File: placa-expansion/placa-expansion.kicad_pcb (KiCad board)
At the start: 2 copper layers, 17 parts, among them J1 PBD-26, P1 BATT, P2 CONN_3PI, P3 PWR_HUB, P4 PWR_3pi, P5 CONN_4, P6 CONN_4, P7 CONN_4, P8 CONN_4, U1 PTN78020

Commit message: Comienzamos a rutear la placa interfaz
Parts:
- U1, U?1: moved to B.Cu
- moved P7 356.5 mm to (338.5, 257.5)
- moved P6 335.6 mm to (370.5, 189.0), turned to 90 degrees
- moved P2 329.2 mm to (338.5, 183.0)
- moved P3 328.8 mm to (366.5, 162.5), turned to 270 degrees
- moved U?1 318.2 mm to (324.0, 234.0), turned to 90 degrees
- moved P8 313.5 mm to (341.0, 151.0)
- moved R1 308.6 mm to (370.5, 173.5), turned to 90 degrees
- moved JP1 299.8 mm to (364.0, 153.5), turned to 90 degrees
- moved R2 293.8 mm to (308.0, 181.0), turned to 90 degrees
- moved D1 285.0 mm to (308.0, 191.5), turned to 90 degrees
- moved P5 280.2 mm to (308.0, 202.0), turned to 90 degrees
- moved C2 276.6 mm to (309.0, 161.5), turned to 180 degrees
- moved C1 273.3 mm to (317.0, 163.0), turned to 180 degrees
- moved P1 272.4 mm to (317.5, 156.0), turned to 180 degrees
- moved P4 262.7 mm to (308.0, 170.0), turned to 270 degrees
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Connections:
- J1 pad 7: (no net) -> /TX_rPi
- P2 pad 11: /PB3 -> /Echo4
- P2 pad 9: /Echo4 -> /PC6
- P4 pad 2: (no net) -> +BATT
- P5 pad 2: /PB3 -> /PC6
- P6 pad 2: /PB3 -> /PC6
- P7 pad 2: /PB3 -> /PC6
- P8 pad 2: /PB3 -> /PC6
- U?1 pad 13: /PB3 -> /PC6
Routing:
- net /TX_3pi: track 0.00 -> 123.6 mm
- net /AD6: track 0.00 -> 104.9 mm
- net /AD7: track 0.00 -> 91.5 mm
- net /Echo3: track 0.00 -> 78.0 mm
- net /RX_3pi: track 0.00 -> 71.1 mm
- net /Vcc_3pi: track 0.00 -> 59.0 mm
- net /Echo4: track 0.00 -> 58.7 mm
- net /PC6: track 0.00 -> 55.0 mm
- net /3v3_rPi: track 0.00 -> 31.3 mm
- net +5V: track 0.00 -> 27.4 mm
- net /TX_rPi: track 0.00 -> 17.0 mm
- net /LED: track 0.00 -> 16.7 mm
- net /PB3_rPi: track 0.00 -> 15.7 mm
- net /PC6_rPi: track 0.00 -> 14.0 mm
- net /AD6_rPi: track 0.00 -> 13.2 mm
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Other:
- board outline added: 139.1 x 220.7 mm
- net class Default: clearance 0.254 -> 0.4064; trace_width 0.254 -> 0.4064
- net class low_mils added: clearance 0.254, trace_width 0.3048, via_dia 0.889, via_drill 0.635
- rule trace_clearance: 0.254 -> 0.4064

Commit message: Pequeña modificacion en el pcb
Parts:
- moved P8 2.06 mm to (343.0, 150.5), turned to 180 degrees
- moved P5 0.50 mm to (308.0, 202.5), turned to 270 degrees
- turned R2 to 270 degrees
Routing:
- net /PC6: track 55.0 -> 319.8 mm
- net +5V: track 27.4 -> 117.4 mm
- net N-0000035: track 0.00 -> 66.8 mm
- net N-0000023: track 0.00 -> 40.1 mm
- net +BATT: track 0.00 -> 28.3 mm
- net N-0000022: track 0.00 -> 13.6 mm
- net /TX_3pi: track 123.6 -> 115.0 mm
- net N-000001: track 0.00 -> 4.15 mm
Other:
- outline, holes or cut-outs redrawn

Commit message: placa routeada
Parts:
- moved R1 201.0 mm to (185.3, 95.4), turned to 0 degrees
- moved C1 154.1 mm to (173.0, 108.1)
- moved C2 154.1 mm to (165.0, 106.6)
- moved D1 154.1 mm to (164.0, 136.6)
- moved J1 154.1 mm to (164.0, 180.6)
- moved P1 154.1 mm to (173.5, 101.1)
- moved P2 154.1 mm to (194.5, 128.1)
- moved P3 154.1 mm to (222.5, 107.6)
- moved P4 154.1 mm to (164.0, 115.1)
- moved P5 154.1 mm to (164.0, 147.6)
- moved P6 154.1 mm to (226.5, 134.1)
- moved P7 154.1 mm to (194.5, 202.6)
- moved P8 154.1 mm to (199.0, 95.6)
- moved R2 154.1 mm to (164.0, 126.1)
- moved U1 154.1 mm to (197.5, 109.1)
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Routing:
- net +5V: track 117.4 -> 269.3 mm, vias 0 -> 5
- net GND: track 0.00 -> 103.5 mm, vias 0 -> 13
- net /PC6: track 319.8 -> 218.2 mm, vias 0 -> 8
- net /Echo4: track 58.7 -> 139.5 mm, vias 0 -> 2
- net N-000002: track 0.00 -> 57.7 mm, vias 0 -> 1
- net /AD6: track 104.9 -> 159.6 mm, vias 0 -> 2
- net N-0000035: track 66.8 -> 30.2 mm
- net N-0000023: track 40.1 -> 7.30 mm
- net N-0000022: track 13.6 -> 44.4 mm
- net /Echo3: track 78.0 -> 105.0 mm, vias 0 -> 2
- net /RX_rPi: track 0.00 -> 16.5 mm
- net /AD7: track 91.5 -> 105.2 mm, vias 0 -> 2
- net /Vcc_3pi: track 59.0 -> 62.1 mm, vias 0 -> 2
- net /TX_3pi: track 115.0 -> 112.1 mm
- added copper zone on B.Cu, net GND
- added copper zone on F.Cu, net GND
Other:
- board size 139.1 x 220.7 mm -> 396.4 x 134.5 mm
- net class Default: clearance 0.4064 -> 0.3048; via_dia 0.889 -> 1.524
- net class low_mils: via_dia 0.889 -> 1.524
- rule trace_clearance: 0.4064 -> 0.3048

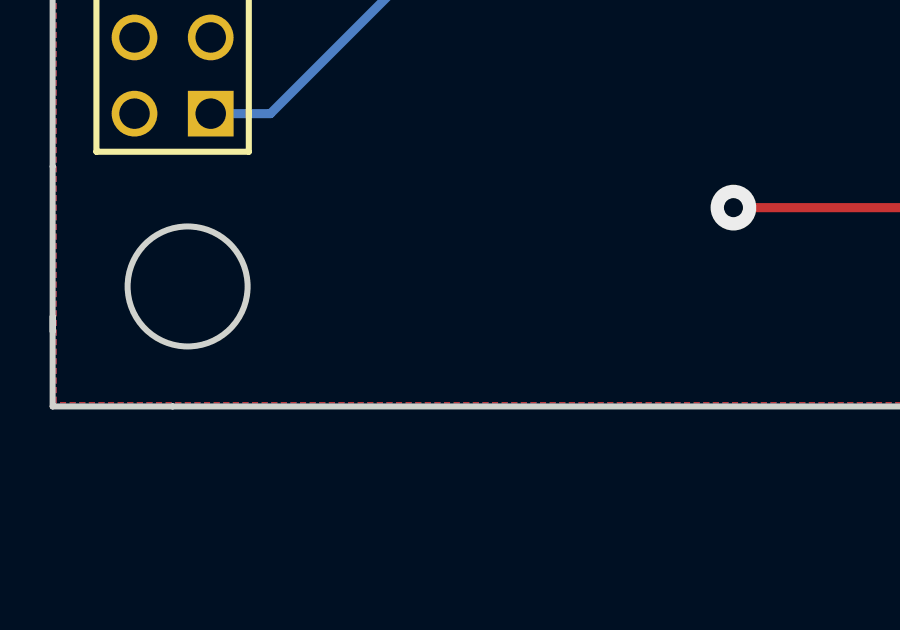
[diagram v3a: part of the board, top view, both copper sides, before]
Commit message: agregue texto a la placa
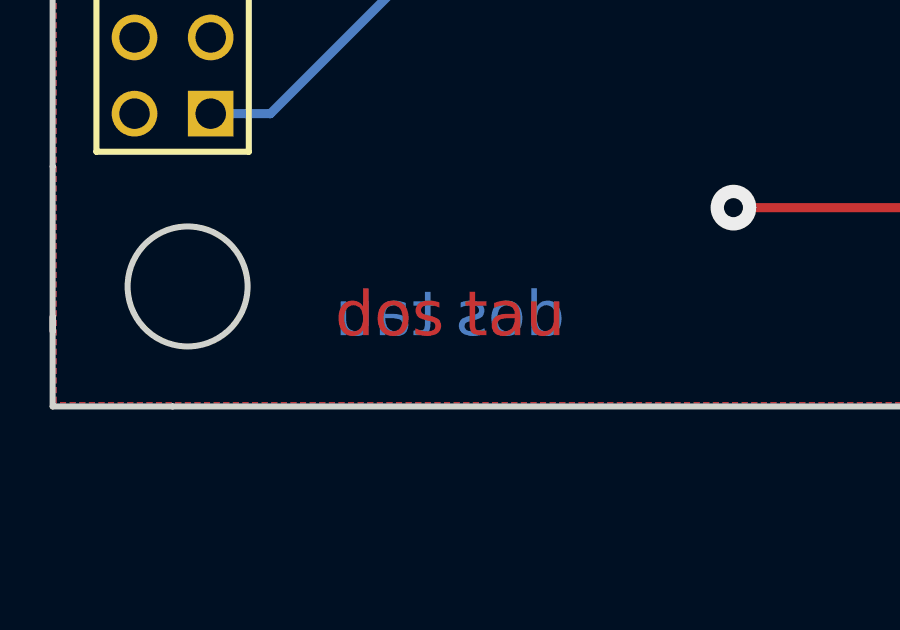
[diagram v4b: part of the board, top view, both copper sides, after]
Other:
- board text added: "dos tau"
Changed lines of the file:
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@@
     (links 59)
     (no_connects 0)
-    (area 232.640199 32.284999 538.580001 260.9544)
+    (area 159.2576 91.035999 573.073201 230.198601)
     (thickness 1.6)
-    (drawings 27)
+    (drawings 29)
     (tracks 270)
     (zones 0)
@@
     (visible_elements 7FFFEFFF)
     (pcbplotparams
-      (layerselection 3178497)
-      (usegerberextensions true)
-      (excludeedgelayer true)
+      (layerselection 32769)
+      (usegerberextensions false)
+      (excludeedgelayer false)
       (linewidth 0.150000)
       (plotframeref false)
@@
       (outputformat 1)
       (mirror false)
-      (drillshape 1)
+      (drillshape 0)
       (scaleselection 1)
       (outputdirectory ""))
@@
     )
   )
+  (gr_text "dos tau" (at 173.228 202.565) (layer F.Cu)
+    (effects (font (size 1.5 1.5) (thickness 0.3)))
+  )
+  (gr_text "dos tau" (at 173.228 202.565) (layer B.Cu)
+    (effects (font (size 1.5 1.5) (thickness 0.3)) (justify mirror))
+  )
   (gr_line (start 159.982 157.136) (end 159.982 160.136) (angle 90) (layer Edge.Cuts) (width 0.2))

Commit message: Borro las pistas y agrando los pads.
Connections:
- J1 pad 2: (no net) -> +5V
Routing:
- net +5V: track 269.3 -> 0.00 mm, vias 5 -> 0
- net /PC6: track 218.2 -> 0.00 mm, vias 8 -> 0
- net /AD6: track 159.6 -> 0.00 mm, vias 2 -> 0
- net /Echo4: track 139.5 -> 0.00 mm, vias 2 -> 0
- net /TX_3pi: track 112.1 -> 0.00 mm
- net /AD7: track 105.2 -> 0.00 mm, vias 2 -> 0
- net /Echo3: track 105.0 -> 0.00 mm, vias 2 -> 0
- net GND: track 103.5 -> 0.00 mm, vias 13 -> 0
- net /RX_3pi: track 71.1 -> 0.00 mm
- net /Vcc_3pi: track 62.1 -> 0.00 mm, vias 2 -> 0
- net N-000005: track 57.7 -> 0.00 mm, vias 1 -> 0
- net N-000001: track 44.4 -> 0.00 mm
- net /3v3_rPi: track 31.3 -> 0.00 mm
- net N-0000040: track 30.2 -> 0.00 mm
- net +BATT: track 28.3 -> 0.00 mm
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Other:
- board size 396.4 x 134.5 mm -> 70 x 114.2 mm
- net class Default: trace_width 0.4064 -> 0.8; via_dia 1.524 -> 2; via_drill 0.635 -> 0.8
- net class low_mils: trace_width 0.3048 -> 0.8; via_dia 1.524 -> 2; via_drill 0.635 -> 0.8

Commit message: subo placa rooteada. Faltaría revisión.
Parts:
- added 1PIN: P***, 1pin, F.Cu at (225.5, 202.1)
- added 1PIN: P***, 1pin, F.Cu at (164.5, 201.7)
- added 1PIN: P***, 1pin, F.Cu at (225.0, 159.1)
- added 1PIN: P***, 1pin, F.Cu at (165.0, 159.1)
- added 1PIN: P***, 1pin, F.Cu at (165.0, 100.2)
- added 1PIN: P***, 1pin, F.Cu at (225.0, 100.1)
- moved C2 55.3 mm to (219.0, 95.0), turned to 0 degrees
- moved JP1 46.7 mm to (173.5, 94.5), turned to 180 degrees
- moved R1 1.41 mm to (184.0, 96.0)
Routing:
- net /PC6: track 0.00 -> 270.9 mm, vias 0 -> 3
- net +5V: track 0.00 -> 240.7 mm, vias 0 -> 3
- net /Echo3: track 0.00 -> 173.0 mm, vias 0 -> 3
- net /Echo4: track 0.00 -> 136.1 mm, vias 0 -> 4
- net /TX_3pi: track 0.00 -> 106.0 mm, vias 0 -> 2
- net /AD7: track 0.00 -> 105.2 mm, vias 0 -> 3
- net /AD6: track 0.00 -> 105.2 mm, vias 0 -> 2
- net /RX_3pi: track 0.00 -> 92.4 mm, vias 0 -> 2
- net /Vcc_3pi: track 0.00 -> 60.3 mm
- net N-000005: track 0.00 -> 54.8 mm
- net N-000001: track 0.00 -> 47.5 mm
- net /RX_rPi: track 0.00 -> 46.4 mm, vias 0 -> 2
- net /3v3_rPi: track 0.00 -> 30.6 mm
- net +BATT: track 0.00 -> 29.4 mm
- net N-0000040: track 0.00 -> 24.5 mm
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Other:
- net class Default: clearance 0.3048 -> 0.508; trace_width 0.8 -> 0.762; via_drill 0.8 -> 0.7
- rule trace_clearance: 0.3048 -> 0.508

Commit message: subo logo a la placa
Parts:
- added G***: LOGO, LOGO, F.Cu at (220.9, 181.9)
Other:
- board text removed: "dos tau"
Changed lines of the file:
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@@
     (links 60)
     (no_connects 1)
-    (area 159.2576 91.149999 231.10022 206.0904)
+    (area 142.028571 90.6 231.30342 206.2936)
     (thickness 1.6)
-    (drawings 11)
+    (drawings 9)
     (tracks 279)
     (zones 0)
-    (modules 23)
+    (modules 24)
     (nets 26)
   )
@@
     (user_trace_width 0.508)
     (trace_clearance 0.508)
-    (zone_clearance 0.3048)
+    (zone_clearance 0.381)
     (zone_45_only no)
     (trace_min 0.254)
@@
     )
   )
+  (module LOGO (layer F.Cu)
+    (at 220.9 181.9 90)
+    (fp_text reference G*** (at 0 6.096 90) (layer F.SilkS) hide
+      (effects (font (thickness 0.3048)))
+    )
+    (fp_text value LOGO (at 0 -6.096 90) (layer F.SilkS) hide
+      (effects (font (thickness 0.3048)))
+    )
+    (fp_poly (pts (xy 13.63218 5.334) (xy 12.45362 5.334) (xy 12.45362 -4.32054) (xy 9.78662 -4.32054)
+      (xy 9.0424 -4.31546) (xy 8.36422 -4.30784) (xy 7.76986 -4.29514) (xy 7.28218 -4.27736)
+      (xy 6.92404 -4.2545) (xy 6.71068 -4.23164) (xy 6.70306 -4.2291) (xy 6.3246 -4.10464)
+      (xy 5.9944 -3.89128) (xy 5.69214 -3.57124) (xy 5.39242 -3.11912) (xy 5.15874 -2.68478)
+      (xy 4.97332 -2.31394) (xy 4.85902 -2.06502) (xy 4.80822 -1.91516) (xy 4.81076 -1.83642)
+      (xy 4.86156 -1.8034) (xy 4.90728 -1.79324) (xy 5.05206 -1.82626) (xy 5.25526 -1.9685)
+      (xy 5.53466 -2.23266) (xy 5.57276 -2.2733) (xy 5.87756 -2.56286) (xy 6.1595 -2.76098)
+      (xy 6.4643 -2.88036) (xy 6.83768 -2.94386) (xy 7.3279 -2.96418) (xy 7.4295 -2.96418)
+      (xy 7.69874 -2.96926) (xy 7.89178 -2.96418) (xy 8.02132 -2.92862) (xy 8.09244 -2.83972)
+      (xy 8.1153 -2.67208) (xy 8.10006 -2.40284) (xy 8.0518 -2.01168) (xy 7.99084 -1.5113)
+      (xy 7.91718 -0.77978) (xy 7.86638 -0.04064) (xy 7.84352 0.67564) (xy 7.84352 1.33858)
+      (xy 7.87146 1.91516) (xy 7.92226 2.37998) (xy 7.98068 2.64414) (xy 8.21436 3.18262)
+      (xy 8.53694 3.5814) (xy 8.9535 3.83794) (xy 9.47166 3.9624) (xy 9.7282 3.9751)
+      (xy 10.09396 3.95986) (xy 10.3759 3.89128) (xy 10.64006 3.76174) (xy 11.03122 3.43662)
+      (xy 11.34872 2.96418) (xy 11.59256 2.3495) (xy 11.73226 1.75514) (xy 11.75766 1.5494)
+      (xy 11.72464 1.45796) (xy 11.6078 1.43764) (xy 11.57986 1.43764) (xy 11.42492 1.47828)
+      (xy 11.29792 1.61798) (xy 11.21156 1.78816) (xy 10.96772 2.14884) (xy 10.62736 2.3749)
+      (xy 10.20826 2.45364) (xy 10.20318 2.45364) (xy 9.77392 2.37998) (xy 9.42848 2.16154)
+      (xy 9.17448 1.81102) (xy 9.02462 1.33858) (xy 9.00176 1.19126) (xy 8.9916 0.92456)
+      (xy 8.99922 0.52324) (xy 9.02716 0.01016) (xy 9.07034 -0.57658) (xy 9.12876 -1.21412)
+      (xy 9.19988 -1.8669) (xy 9.24306 -2.2225) (xy 9.3345 -2.96164) (xy 10.86866 -2.9845)
+      (xy 12.40282 -3.00736) (xy 12.42822 -3.66268) (xy 12.45362 -4.32054) (xy 12.45362 5.334)
+      (xy 2.1082 5.334) (xy 2.1082 -1.31318) (xy 1.92278 -1.3716) (xy 1.75514 -1.42494)
+      (xy 1.47828 -1.50876) (xy 1.14554 -1.60782) (xy 1.05918 -1.63576) (xy 0.381 -1.83642)
+      (xy 1.143 -2.06756) (xy 1.48844 -2.1717) (xy 1.77546 -2.25806) (xy 1.96596 -2.31648)
+      (xy 2.01168 -2.33172) (xy 2.05486 -2.39776) (xy 2.01422 -2.56032) (xy 1.9304 -2.75082)
+      (xy 1.81102 -2.96926) (xy 1.7145 -3.10896) (xy 1.67894 -3.13436) (xy 1.58496 -3.09372)
+      (xy 1.37668 -2.97942) (xy 1.0922 -2.81686) (xy 0.8382 -2.66446) (xy 0.5207 -2.47396)
+      (xy 0.26162 -2.32664) (xy 0.09398 -2.23774) (xy 0.04064 -2.21996) (xy 0.04318 -2.30886)
+      (xy 0.06604 -2.5273) (xy 0.10922 -2.83464) (xy 0.13462 -3.00736) (xy 0.18542 -3.35026)
+      (xy 0.22606 -3.62712) (xy 0.24892 -3.79984) (xy 0.25146 -3.83286) (xy 0.17526 -3.86842)
+      (xy -0.02032 -3.89128) (xy -0.21336 -3.89636) (xy -0.48006 -3.89128) (xy -0.61214 -3.86588)
+      (xy -0.65278 -3.79984) (xy -0.64008 -3.70586) (xy -0.59944 -3.48996) (xy -0.55626 -3.2004)
+      (xy -0.51562 -2.8829) (xy -0.4826 -2.58572) (xy -0.46228 -2.35204) (xy -0.45974 -2.22758)
+      (xy -0.46228 -2.21996) (xy -0.54102 -2.25044) (xy -0.73406 -2.35458) (xy -1.00838 -2.51714)
+      (xy -1.3081 -2.70256) (xy -2.1209 -3.21564) (xy -2.30632 -2.83718) (xy -2.41046 -2.57302)
+      (xy -2.4257 -2.40792) (xy -2.40792 -2.37998) (xy -2.29616 -2.3241) (xy -2.06248 -2.2352)
+      (xy -1.74752 -2.12852) (xy -1.56718 -2.07264) (xy -0.80518 -1.83896) (xy -1.60782 -1.5875)
+      (xy -1.95072 -1.48082) (xy -2.22758 -1.38938) (xy -2.40284 -1.32842) (xy -2.44348 -1.31064)
+      (xy -2.43586 -1.2192) (xy -2.37744 -1.03632) (xy -2.29362 -0.81788) (xy -2.20472 -0.62484)
+      (xy -2.13614 -0.51562) (xy -2.12344 -0.508) (xy -2.032 -0.55118) (xy -1.8288 -0.66548)
+      (xy -1.54432 -0.83312) (xy -1.23444 -1.02108) (xy -0.40386 -1.53416) (xy -0.45212 -1.25476)
+      (xy -0.49276 -0.99568) (xy -0.53594 -0.67564) (xy -0.55118 -0.55118) (xy -0.58928 -0.26162)
+      (xy -0.62738 -0.01524) (xy -0.64262 0.0635) (xy -0.65278 0.17018) (xy -0.59944 0.2286)
+      (xy -0.4445 0.24892) (xy -0.21336 0.254) (xy 0.08128 0.23876) (xy 0.2286 0.1905)
+      (xy 0.254 0.14224) (xy 0.23876 0.00254) (xy 0.20574 -0.24384) (xy 0.16764 -0.47244)
+      (xy 0.11176 -0.8001) (xy 0.06096 -1.10236) (xy 0.03556 -1.24968) (xy -0.00762 -1.524)
+      (xy 0.84836 -1.00838) (xy 1.18364 -0.81026) (xy 1.46304 -0.65278) (xy 1.65862 -0.55118)
+      (xy 1.73736 -0.52578) (xy 1.78816 -0.61468) (xy 1.8796 -0.80772) (xy 1.94056 -0.93472)
+      (xy 2.1082 -1.31318) (xy 2.1082 5.334) (xy 0.04318 5.334) (xy -6.62178 5.334)
+      (xy -6.62178 -2.48158) (xy -6.65734 -2.81178) (xy -6.6802 -2.8956) (xy -6.87578 -3.24866)
+      (xy -7.19074 -3.5687) (xy -7.58444 -3.80492) (xy -7.69366 -3.85064) (xy -8.001 -3.91922)
+      (xy -8.42264 -3.95986) (xy -8.90524 -3.97256) (xy -9.40054 -3.95732) (xy -9.85266 -3.91414)
+      (xy -10.11682 -3.86588) (xy -10.53846 -3.76936) (xy -10.64006 -3.175) (xy -10.7061 -2.78384)
+      (xy -10.73658 -2.5273) (xy -10.73404 -2.37744) (xy -10.69086 -2.30886) (xy -10.6045 -2.28854)
+      (xy -10.56132 -2.286) (xy -10.43432 -2.32156) (xy -10.32764 -2.44602) (xy -10.21334 -2.69748)
+      (xy -10.1981 -2.7305) (xy -10.04824 -3.03784) (xy -9.8552 -3.24358) (xy -9.58342 -3.37058)
+      (xy -9.1948 -3.43916) (xy -8.9662 -3.45694) (xy -8.56996 -3.45948) (xy -8.28294 -3.41122)
+      (xy -8.13562 -3.34772) (xy -7.8613 -3.11658) (xy -7.69366 -2.77368) (xy -7.63016 -2.33934)
+      (xy -7.67334 -1.83642) (xy -7.82574 -1.28778) (xy -8.001 -0.8763) (xy -8.20674 -0.51308)
+      (xy -8.46074 -0.15748) (xy -8.7884 0.2032) (xy -9.20242 0.59182) (xy -9.72058 1.02362)
+      (xy -10.36066 1.51384) (xy -10.62482 1.70942) (xy -11.09218 2.05486) (xy -11.43762 2.32156)
+      (xy -11.68146 2.53238) (xy -11.84148 2.70764) (xy -11.938 2.86766) (xy -11.9888 3.0353)
+      (xy -12.00912 3.22834) (xy -12.0142 3.27914) (xy -12.02182 3.46964) (xy -9.73582 3.46964)
+      (xy -9.02208 3.4671) (xy -8.46328 3.46202) (xy -8.04164 3.45186) (xy -7.747 3.43662)
+      (xy -7.55904 3.4163) (xy -7.4676 3.38836) (xy -7.44982 3.3655) (xy -7.43712 3.21564)
+      (xy -7.4041 2.9845) (xy -7.39648 2.94132) (xy -7.34568 2.62636) (xy -9.1821 2.6035)
+      (xy -11.01852 2.58064) (xy -10.0711 1.91262) (xy -9.22528 1.29794) (xy -8.52424 0.74422)
+      (xy -7.9502 0.23622) (xy -7.49554 -0.23368) (xy -7.1501 -0.6858) (xy -6.89864 -1.12776)
+      (xy -6.73354 -1.57226) (xy -6.6421 -2.03708) (xy -6.63448 -2.09804) (xy -6.62178 -2.48158)
+      (xy -6.62178 5.334) (xy -13.54582 5.334) (xy -13.54582 0) (xy -13.54582 -5.334)
+      (xy 0.04318 -5.334) (xy 13.63218 -5.334) (xy 13.63218 0) (xy 13.63218 5.334)
+      (xy 13.63218 5.334)) (layer F.Cu) (width 0.00254))
+  )
   (gr_line (start 160 205.5) (end 160 91.25) (angle 90) (layer Edge.Cuts) (width 0.2))
   (gr_line (start 230 205.5) (end 160 205.5) (angle 90) (layer Edge.Cuts) (width 0.2))
   (gr_line (start 230 91.25) (end 230 205.5) (angle 90) (layer Edge.Cuts) (width 0.2))
   (gr_line (start 160 91.25) (end 230 91.25) (angle 90) (layer Edge.Cuts) (width 0.2))
-  (gr_text "dos tau" (at 146.5 196.5) (layer F.Cu)
-    (effects (font (size 1.5 1.5) (thickness 0.3)))
-  )
-  (gr_text "dos tau" (at 147.5 199.5) (layer B.Cu)
-    (effects (font (size 1.5 1.5) (thickness 0.3)) (justify mirror))
-  )
   (gr_line (start 159.982 157.136) (end 159.982 160.136) (angle 90) (layer Edge.Cuts) (width 0.2))
   (gr_line (start 223.474 198.684) (end 167.594 198.684) (angle 90) (layer Dwgs.User) (width 0.2))
@@
       )
     )
+  )
+  (zone (net 0) (net_name "") (layer F.Cu) (hatch edge 0.508)
+    (connect_pads (clearance 0.381))
+    (min_thickness 0.254)
+    (keepout (tracks not_allowed) (vias not_allowed) (copperpour not_allowed))
+    (fill (arc_segments 16) (thermal_gap 0.508) (thermal_bridge_width 0.508))
+    (polygon
+      (pts
+        (xy 225.2 194.9) (xy 215.9 194.8) (xy 215.8 169) (xy 225.6 169)
+      )
+    )
